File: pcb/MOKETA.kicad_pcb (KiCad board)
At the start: 2 copper layers, 144.9 x 166.3 mm, 129 parts, among them SW43 Reset, U1 Pro_Micro

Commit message: fix
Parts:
- moved SW12 187.8 mm to (317.3, 114.4), turned to 15 degrees
- moved SW11 162.5 mm to (297.1, 112.3), turned to 15 degrees
- moved SW24 148.2 mm to (322.2, 132.7), turned to 15 degrees
- moved SW25 140.8 mm to (79.3, 151.1), turned to -15 degrees
- moved SW10 137.7 mm to (276.9, 110.4), turned to 15 degrees
- moved SW37 132.5 mm to (150.3, 179.8), turned to -15 degrees
- moved SW23 123.2 mm to (302.0, 130.7), turned to 15 degrees
- moved SW9 114.3 mm to (257.3, 110.8), turned to 15 degrees
- moved SW26 113.1 mm to (99.5, 149.0), turned to -15 degrees
- moved SW38 111.0 mm to (168.0, 187.1), turned to -15 degrees
- moved SW36 108.7 mm to (327.1, 151.1), turned to 15 degrees
- moved U1 107.2 mm to (203.2, 116.0)
- moved SW22 99.1 mm to (281.8, 128.8), turned to 15 degrees
- moved SW8 97.0 mm to (240.2, 120.3), turned to 15 degrees
- moved SW13 92.3 mm to (84.2, 132.7), turned to -15 degrees
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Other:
- board size 144.9 x 166.3 mm -> 280 x 115 mm

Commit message: add outline
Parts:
- added SW44: ~, moketa:BSI-10H, F.Cu at (340.2, 157.3)
- moved LED12 222.3 mm to (318.6, 119.3), turned to 15 degrees
- moved LED24 218.1 mm to (323.5, 137.7), turned to 15 degrees
- moved LED36 214.0 mm to (328.4, 156.0), turned to 15 degrees
- moved LED11 202.3 mm to (298.4, 117.3), turned to 15 degrees
- moved LED23 198.0 mm to (303.3, 135.6), turned to 15 degrees
- moved LED35 193.9 mm to (308.2, 153.9), turned to 15 degrees
- moved LED9 183.7 mm to (258.6, 115.7), turned to 15 degrees
- moved LED10 182.4 mm to (278.2, 115.4), turned to 15 degrees
- moved LED22 178.0 mm to (283.1, 133.7), turned to 15 degrees
- moved LED34 173.8 mm to (288.0, 152.1), turned to 15 degrees
- moved LED8 162.2 mm to (241.5, 125.2), turned to 15 degrees
- moved LED21 158.0 mm to (263.5, 134.0), turned to 15 degrees
- moved LED33 153.7 mm to (268.5, 152.4), turned to 15 degrees
- moved LED7 140.5 mm to (225.0, 136.9), turned to 15 degrees
- moved LED20 138.0 mm to (246.4, 143.6), turned to 15 degrees
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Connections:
- LED37 pad 3: unconnected-(LED37-VSS-Pad3) -> GND
- LED42 pad 3: unconnected-(LED42-VSS-Pad3) -> GND
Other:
- board size 280 x 115 mm -> 283.8 x 114.8 mm

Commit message: Basic routing
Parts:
- moved SW42 39.2 mm to (256.1, 177.6)
- moved LED42 39.2 mm to (257.4, 182.5)
- moved SW40 37.5 mm to (220.7, 192.2)
- moved LED40 37.5 mm to (222.0, 197.1)
- moved D16 8.12 mm to (138.8, 117.7), turned to 75 degrees
- moved D4 8.12 mm to (143.7, 99.4), turned to 75 degrees
- moved D29 8.12 mm to (151.0, 145.6), turned to 75 degrees
- moved D2 8.12 mm to (104.0, 100.9), turned to 75 degrees
- moved D6 8.12 mm to (177.4, 120.6), turned to 75 degrees
- moved D26 8.12 mm to (94.1, 137.6), turned to 75 degrees
- moved D18 8.12 mm to (172.5, 139.0), turned to 75 degrees
- moved D14 8.12 mm to (99.1, 119.3), turned to 75 degrees
- moved D17 8.12 mm to (155.9, 127.2), turned to 75 degrees
- moved D28 8.12 mm to (133.9, 136.1), turned to 75 degrees
- moved D30 8.12 mm to (167.6, 157.3), turned to 75 degrees
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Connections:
- LED39 pad 1: Net-(LED39-VDD) -> VCC
- LED40 pad 1: Net-(LED39-VDD) -> VCC
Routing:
- net VCC: track 0.00 -> 882.2 mm
- net C0: track 0.00 -> 256.9 mm, vias 0 -> 8
- net C1: track 0.00 -> 251.1 mm, vias 0 -> 7
- net C2: track 0.00 -> 249.0 mm, vias 0 -> 8
- net C4: track 0.00 -> 248.9 mm, vias 0 -> 8
- net C5: track 0.00 -> 245.2 mm, vias 0 -> 7
- net C3: track 0.00 -> 245.0 mm, vias 0 -> 7
- net R4: track 0.00 -> 129.4 mm
- net R0: track 0.00 -> 128.2 mm
- net R2: track 0.00 -> 127.4 mm
- net R1: track 0.00 -> 117.5 mm
- net R5: track 0.00 -> 116.4 mm
- net R3: track 0.00 -> 113.6 mm
- net R6: track 0.00 -> 96.6 mm
- net Net-(LED36-DIN): track 0.00 -> 90.5 mm
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- added copper zone on B.Cu, net GND
- added copper zone on F.Cu, net GND
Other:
- outline, holes or cut-outs redrawn

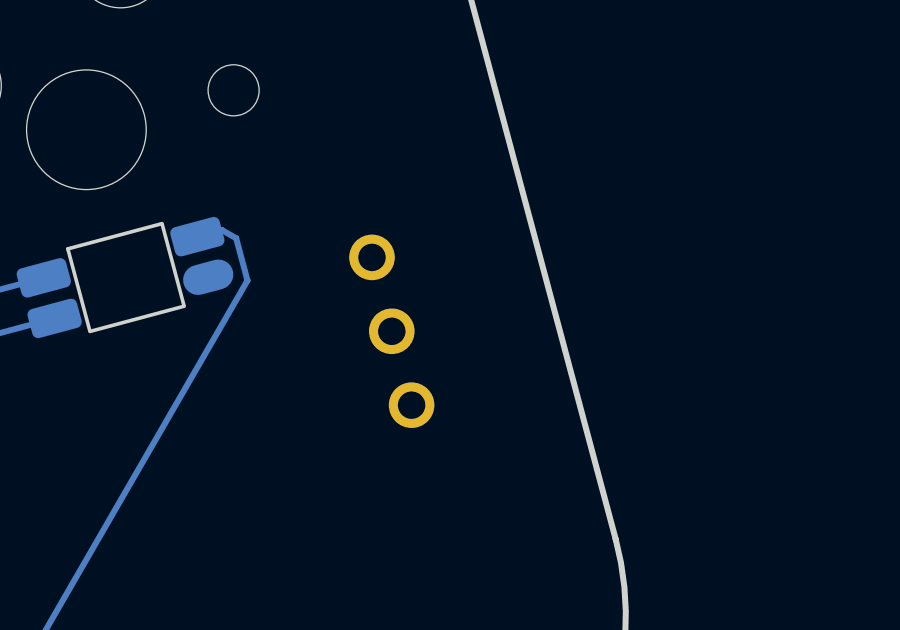
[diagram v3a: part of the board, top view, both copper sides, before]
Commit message: change footrpint
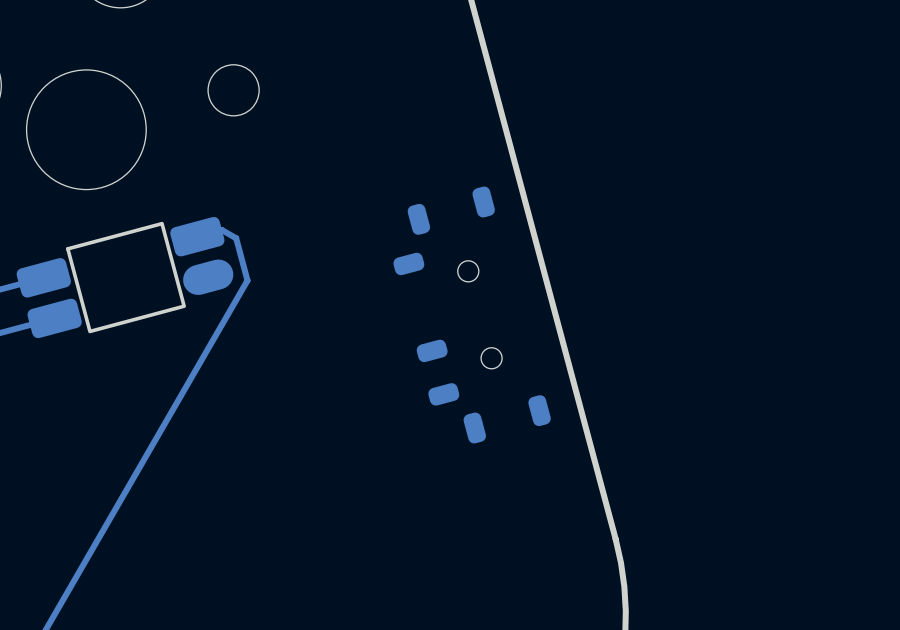
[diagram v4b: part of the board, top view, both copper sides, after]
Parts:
- SW44: footprint moketa:BSI-10H -> moketa:MSK-12C02

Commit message: add footrpint
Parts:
- added D43: ~, moketa:LED_1206, F.Cu at (63.3, 199.6)
- added D44: ~, moketa:LED_1206, F.Cu at (63.3, 203.0)
- added D45: ~, moketa:LED_1206, F.Cu at (63.3, 206.4)
- added D46: ~, moketa:LED_1206, F.Cu at (63.3, 209.8)
- added J2: ~, moketa:FFC_CMD_1x20_P0.5mm, F.Cu at (69.2, 192.3)
- added J3: ~, moketa:FFC_CMD_1x20_P0.5mm, F.Cu at (69.2, 197.1)
- added R1: ~, moketa:R_1206_3216, F.Cu at (69.2, 199.5)
- added R2: ~, moketa:R_1206_3216, F.Cu at (69.2, 202.9)
- added R3: ~, moketa:R_1206_3216, F.Cu at (69.2, 206.2)
- added R4: ~, moketa:R_1206_3216, F.Cu at (69.2, 209.5)
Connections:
- net LED renamed LEDS
- U1 pad 11: unconnected-(U1-8/B4-Pad11) -> LED2
- U1 pad 12: unconnected-(U1-9/B5-Pad12) -> LED3
- U1 pad 14: unconnected-(U1-B2/16-Pad14) -> LED4
- U1 pad 2: unconnected-(U1-RX1/D2-Pad2) -> LED1

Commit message: Doter pcb base cut
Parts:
- moved J3 147.6 mm to (203.2, 135.3)
- moved SW44 136.0 mm to (218.4, 94.6), turned to 0 degrees
- moved J2 135.2 mm to (203.6, 177.4), turned to 180 degrees
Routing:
- net C1: track 251.1 -> 231.9 mm
- net R1: track 117.5 -> 110.0 mm
- net C0: track 256.9 -> 249.7 mm
- net C3: track 245.0 -> 249.6 mm
- net R0: track 128.2 -> 123.9 mm
- net C2: track 249.0 -> 252.6 mm
- net R3: track 113.6 -> 117.1 mm
- net VCC: track 882.2 -> 884.3 mm
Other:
- outline, holes or cut-outs redrawn

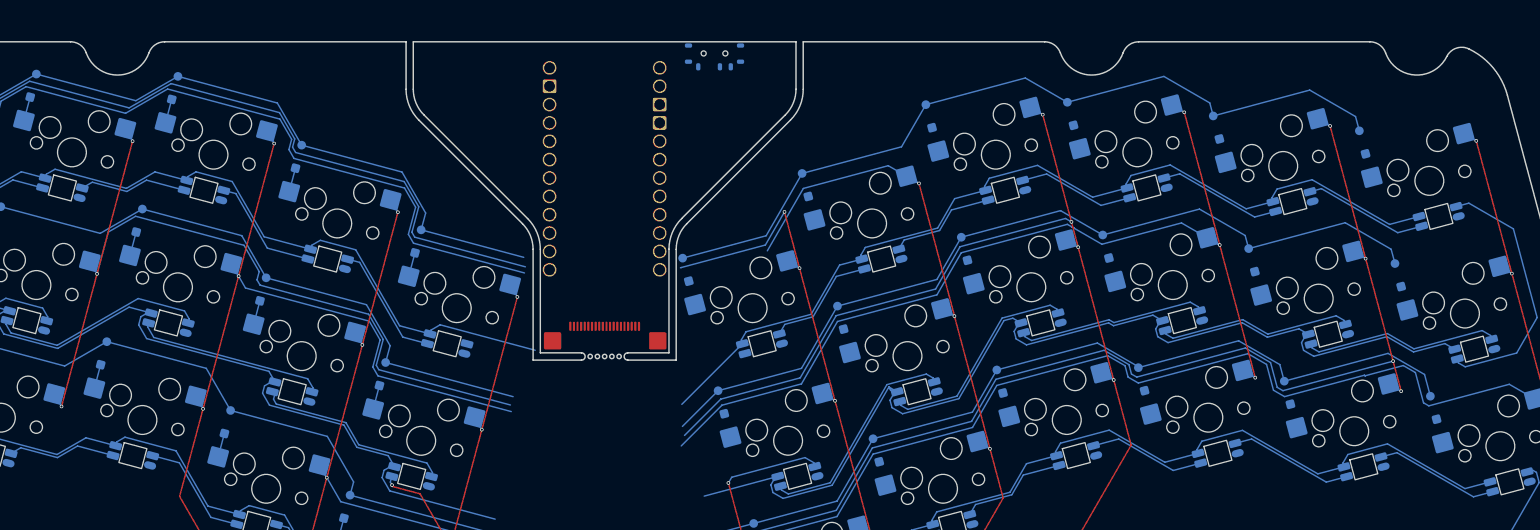
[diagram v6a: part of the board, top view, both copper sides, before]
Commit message: update footptint
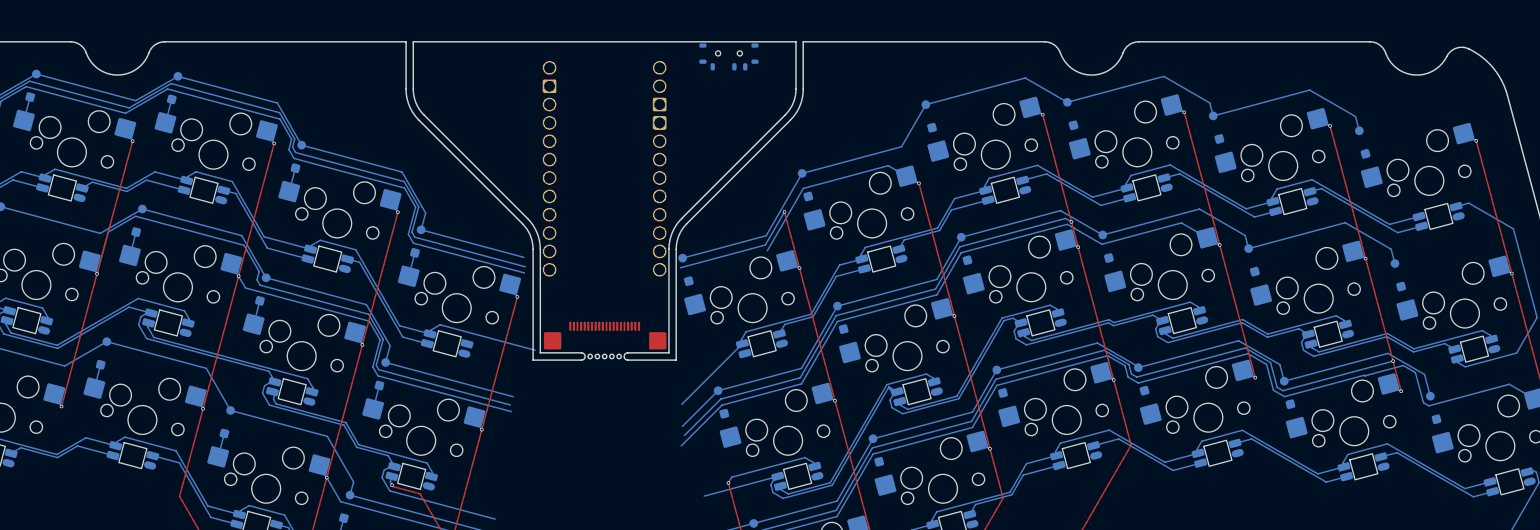
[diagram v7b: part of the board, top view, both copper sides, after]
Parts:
- moved SW44 2.00 mm to (220.4, 94.6)

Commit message: Basic routing on almost whole board
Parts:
- moved D46 283.3 mm to (332.7, 122.0), turned to 105 degrees
- moved D45 282.6 mm to (331.3, 116.7), turned to 105 degrees
- moved D44 281.9 mm to (329.9, 111.4), turned to 105 degrees
- moved D43 281.2 mm to (328.4, 106.1), turned to 105 degrees
- moved R4 244.3 mm to (311.2, 175.9), turned to 15 degrees
- moved R3 243.4 mm to (310.3, 172.3), turned to 15 degrees
- moved R2 242.5 mm to (309.3, 168.8), turned to 15 degrees
- moved R1 241.6 mm to (308.3, 165.2), turned to 15 degrees
- moved SW43 102.5 mm to (183.8, 98.2), turned to -120 degrees
- moved J1 60.7 mm to (203.5, 134.6)
- moved D40 38.3 mm to (211.5, 186.9)
- moved D42 38.3 mm to (246.9, 172.3)
- moved J2 0.35 mm to (203.2, 177.4)
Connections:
- D1 pad 1: R0 -> R0P
- D10 pad 1: R1 -> R1P
- D11 pad 1: R1 -> R1P
- D12 pad 1: R1 -> R1P
- D13 pad 1: R2 -> R2P
- D14 pad 1: R2 -> R2P
- D15 pad 1: R2 -> R2P
- D16 pad 1: R2 -> R2P
- D17 pad 1: R2 -> R2P
- D18 pad 1: R2 -> R2P
- D19 pad 1: R3 -> R3P
- D2 pad 1: R0 -> R0P
- D20 pad 1: R3 -> R3P
- D21 pad 1: R3 -> R3P
- D22 pad 1: R3 -> R3P
- D23 pad 1: R3 -> R3P
- D24 pad 1: R3 -> R3P
- D25 pad 1: R4 -> R4P
- D26 pad 1: R4 -> R4P
- D27 pad 1: R4 -> R4P
- D28 pad 1: R4 -> R4P
- D29 pad 1: R4 -> R4P
- D3 pad 1: R0 -> R0P
- D30 pad 1: R4 -> R4P
- D31 pad 1: R5 -> R5P
- D32 pad 1: R5 -> R5P
- D33 pad 1: R5 -> R5P
- D34 pad 1: R5 -> R5P
- D35 pad 1: R5 -> R5P
- D36 pad 1: R5 -> R5P
- D37 pad 1: R6 -> R6P
- D38 pad 1: R6 -> R6P
- D39 pad 1: R6 -> R6P
- D4 pad 1: R0 -> R0P
- D40 pad 1: R6 -> R6P
- D41 pad 1: R6 -> R6P
- D42 pad 1: R6 -> R6P
- D43 pad 1: GND -> GNDP
- D44 pad 1: GND -> GNDP
- D45 pad 1: GND -> GNDP
- D46 pad 1: GND -> GNDP
- D5 pad 1: R0 -> R0P
- D6 pad 1: R0 -> R0P
- D7 pad 1: R1 -> R1P
- D8 pad 1: R1 -> R1P
- D9 pad 1: R1 -> R1P
- J2 pad 1: unconnected-(J2-Pin_1-Pad1) -> LED3P
- J2 pad 10: unconnected-(J2-Pin_10-Pad10) -> LED1P
- J2 pad 11: unconnected-(J2-Pin_11-Pad11) -> LEDSP
- J2 pad 12: unconnected-(J2-Pin_12-Pad12) -> VCCP
- J2 pad 13: unconnected-(J2-Pin_13-Pad13) -> R1P
- J2 pad 14: unconnected-(J2-Pin_14-Pad14) -> R3P
- J2 pad 15: unconnected-(J2-Pin_15-Pad15) -> R5P
- J2 pad 16: unconnected-(J2-Pin_16-Pad16) -> C3P
- J2 pad 17: unconnected-(J2-Pin_17-Pad17) -> C4P
- J2 pad 18: unconnected-(J2-Pin_18-Pad18) -> C5P
- J2 pad 19: unconnected-(J2-Pin_19-Pad19) -> LED4P
- J2 pad 2: unconnected-(J2-Pin_2-Pad2) -> LED2P
- J2 pad 20: unconnected-(J2-Pin_20-Pad20) -> R6P
- J2 pad 3: unconnected-(J2-Pin_3-Pad3) -> C2P
- J2 pad 4: unconnected-(J2-Pin_4-Pad4) -> C1P
- J2 pad 5: unconnected-(J2-Pin_5-Pad5) -> C0P
- J2 pad 6: unconnected-(J2-Pin_6-Pad6) -> R4P
- J2 pad 7: unconnected-(J2-Pin_7-Pad7) -> R2P
- J2 pad 8: unconnected-(J2-Pin_8-Pad8) -> R0P
- J2 pad 9: unconnected-(J2-Pin_9-Pad9) -> GNDP
- J3 pad 1: unconnected-(J3-Pin_1-Pad1) -> R6D
- J3 pad 10: unconnected-(J3-Pin_10-Pad10) -> LEDSD
- J3 pad 11: unconnected-(J3-Pin_11-Pad11) -> LED1D
- J3 pad 12: unconnected-(J3-Pin_12-Pad12) -> GNDD
- J3 pad 13: unconnected-(J3-Pin_13-Pad13) -> R0D
- J3 pad 14: unconnected-(J3-Pin_14-Pad14) -> R2D
- J3 pad 15: unconnected-(J3-Pin_15-Pad15) -> R4D
- J3 pad 16: unconnected-(J3-Pin_16-Pad16) -> C0D
- J3 pad 17: unconnected-(J3-Pin_17-Pad17) -> C1D
- J3 pad 18: unconnected-(J3-Pin_18-Pad18) -> C2D
- J3 pad 19: unconnected-(J3-Pin_19-Pad19) -> LED2D
- J3 pad 2: unconnected-(J3-Pin_2-Pad2) -> LED4D
- J3 pad 20: unconnected-(J3-Pin_20-Pad20) -> LED3D
- J3 pad 3: unconnected-(J3-Pin_3-Pad3) -> C5D
- J3 pad 4: unconnected-(J3-Pin_4-Pad4) -> C4D
- J3 pad 5: unconnected-(J3-Pin_5-Pad5) -> C3D
- J3 pad 6: unconnected-(J3-Pin_6-Pad6) -> R5D
- J3 pad 7: unconnected-(J3-Pin_7-Pad7) -> R3D
- J3 pad 8: unconnected-(J3-Pin_8-Pad8) -> R1D
- J3 pad 9: unconnected-(J3-Pin_9-Pad9) -> VCCD
- LED1 pad 1: VCC -> VCCP
- LED1 pad 3: GND -> GNDP
- LED10 pad 1: VCC -> VCCP
- LED10 pad 3: GND -> GNDP
- LED11 pad 1: VCC -> VCCP
- LED11 pad 3: GND -> GNDP
- LED12 pad 1: VCC -> VCCP
- LED12 pad 3: GND -> GNDP
- LED13 pad 1: VCC -> VCCP
- LED13 pad 3: GND -> GNDP
- LED14 pad 1: VCC -> VCCP
- LED14 pad 3: GND -> GNDP
- LED15 pad 1: VCC -> VCCP
- LED15 pad 3: GND -> GNDP
- LED16 pad 1: VCC -> VCCP
- LED16 pad 3: GND -> GNDP
- LED17 pad 1: VCC -> VCCP
- LED17 pad 3: GND -> GNDP
- LED18 pad 1: VCC -> VCCP
- LED18 pad 3: GND -> GNDP
- LED19 pad 1: VCC -> VCCP
- LED19 pad 3: GND -> GNDP
- LED2 pad 1: VCC -> VCCP
- LED2 pad 3: GND -> GNDP
- LED20 pad 1: VCC -> VCCP
- LED20 pad 3: GND -> GNDP
- LED21 pad 1: VCC -> VCCP
- LED21 pad 3: GND -> GNDP
- LED22 pad 1: VCC -> VCCP
- LED22 pad 3: GND -> GNDP
- LED23 pad 1: VCC -> VCCP
- LED23 pad 3: GND -> GNDP
- LED24 pad 1: VCC -> VCCP
- LED24 pad 3: GND -> GNDP
- LED25 pad 1: VCC -> VCCP
- LED25 pad 3: GND -> GNDP
- LED26 pad 1: VCC -> VCCP
- LED26 pad 3: GND -> GNDP
- LED27 pad 1: VCC -> VCCP
- LED27 pad 3: GND -> GNDP
- LED28 pad 1: VCC -> VCCP
- LED28 pad 3: GND -> GNDP
- LED29 pad 1: VCC -> VCCP
- LED29 pad 3: GND -> GNDP
- LED3 pad 1: VCC -> VCCP
- LED3 pad 3: GND -> GNDP
- LED30 pad 1: VCC -> VCCP
- LED30 pad 3: GND -> GNDP
- LED31 pad 1: VCC -> VCCP
- LED31 pad 3: GND -> GNDP
- LED32 pad 1: VCC -> VCCP
- LED32 pad 3: GND -> GNDP
- LED33 pad 1: VCC -> VCCP
- LED33 pad 3: GND -> GNDP
- LED34 pad 1: VCC -> VCCP
- LED34 pad 3: GND -> GNDP
- LED35 pad 1: VCC -> VCCP
- LED35 pad 3: GND -> GNDP
- LED36 pad 1: VCC -> VCCP
- LED36 pad 3: GND -> GNDP
- LED37 pad 1: VCC -> VCCP
- LED37 pad 3: GND -> GNDP
- LED38 pad 1: VCC -> VCCP
- LED38 pad 3: GND -> GNDP
- LED39 pad 1: VCC -> VCCP
- LED39 pad 3: GND -> GNDP
- LED4 pad 1: VCC -> VCCP
- LED4 pad 3: GND -> GNDP
- LED40 pad 1: VCC -> VCCP
- LED40 pad 3: GND -> GNDP
- LED41 pad 1: VCC -> VCCP
- LED41 pad 3: GND -> GNDP
- LED42 pad 1: VCC -> VCCP
- LED42 pad 3: GND -> GNDP
- LED5 pad 1: VCC -> VCCP
- LED5 pad 3: GND -> GNDP
- LED6 pad 1: VCC -> VCCP
- LED6 pad 3: GND -> GNDP
- LED6 pad 4: LEDS -> LEDSP
- LED7 pad 1: VCC -> VCCP
- LED7 pad 3: GND -> GNDP
- LED8 pad 1: VCC -> VCCP
- LED8 pad 3: GND -> GNDP
- LED9 pad 1: VCC -> VCCP
- LED9 pad 3: GND -> GNDP
- R1 pad 1: LED1 -> LED1P
- R2 pad 1: LED2 -> LED2P
- R3 pad 1: LED3 -> LED3P
- R4 pad 1: LED4 -> LED4P
- SW1 pad 1: C0 -> C0P
- SW10 pad 1: C3 -> C3P
- SW11 pad 1: C4 -> C4P
- SW12 pad 1: C5 -> C5P
- SW13 pad 1: C0 -> C0P
- SW14 pad 1: C1 -> C1P
- SW15 pad 1: C2 -> C2P
- SW16 pad 1: C3 -> C3P
- SW17 pad 1: C4 -> C4P
- SW18 pad 1: C5 -> C5P
- SW19 pad 1: C0 -> C0P
- SW2 pad 1: C1 -> C1P
- SW20 pad 1: C1 -> C1P
- SW21 pad 1: C2 -> C2P
- SW22 pad 1: C3 -> C3P
- SW23 pad 1: C4 -> C4P
- SW24 pad 1: C5 -> C5P
- SW25 pad 1: C0 -> C0P
- SW26 pad 1: C1 -> C1P
- SW27 pad 1: C2 -> C2P
- SW28 pad 1: C3 -> C3P
- SW29 pad 1: C4 -> C4P
- SW3 pad 1: C2 -> C2P
- SW30 pad 1: C5 -> C5P
- SW31 pad 1: C0 -> C0P
- SW32 pad 1: C1 -> C1P
- SW33 pad 1: C2 -> C2P
- SW34 pad 1: C3 -> C3P
- SW35 pad 1: C4 -> C4P
- SW36 pad 1: C5 -> C5P
- SW37 pad 1: C3 -> C3P
- SW38 pad 1: C4 -> C4P
- SW39 pad 1: C5 -> C5P
- SW4 pad 1: C3 -> C3P
- SW40 pad 1: C0 -> C0P
- SW41 pad 1: C1 -> C1P
- SW42 pad 1: C2 -> C2P
- SW5 pad 1: C4 -> C4P
- SW6 pad 1: C5 -> C5P
- SW7 pad 1: C0 -> C0P
- SW8 pad 1: C1 -> C1P
- SW9 pad 1: C2 -> C2P
- U1 pad 1: LEDS -> LEDSD
- U1 pad 10: C2 -> C2D
- U1 pad 11: LED2 -> LED2D
- U1 pad 12: LED3 -> LED3D
- U1 pad 13: R6 -> R6D
- U1 pad 14: LED4 -> LED4D
- U1 pad 15: C5 -> C5D
- U1 pad 16: C4 -> C4D
- U1 pad 17: C3 -> C3D
- U1 pad 18: R5 -> R5D
- U1 pad 19: R3 -> R3D
- U1 pad 2: LED1 -> LED1D
- U1 pad 20: R1 -> R1D
- U1 pad 21: VCC -> VCCD
- U1 pad 3: GND -> GNDD
- U1 pad 4: GND -> GNDD
- U1 pad 5: R0 -> R0D
- U1 pad 6: R2 -> R2D
- U1 pad 7: R4 -> R4D
- U1 pad 8: C0 -> C0D
- U1 pad 9: C1 -> C1D
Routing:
- net VCCP: track 0.00 -> 1174.4 mm, vias 0 -> 1
- net VCC: track 884.3 -> 0.00 mm
- net C0P: track 0.00 -> 352.2 mm, vias 0 -> 9
- net C1P: track 0.00 -> 345.8 mm, vias 0 -> 8
- net C2P: track 0.00 -> 325.6 mm, vias 0 -> 9
- net C3P: track 0.00 -> 321.0 mm, vias 0 -> 8
- net C4P: track 0.00 -> 301.5 mm, vias 0 -> 9
- net C5P: track 0.00 -> 295.8 mm, vias 0 -> 8
- net C2: track 252.6 -> 0.00 mm, vias 8 -> 0
- net C0: track 249.7 -> 0.00 mm, vias 8 -> 0
- net C3: track 249.6 -> 0.00 mm, vias 7 -> 0
- net C4: track 248.9 -> 0.00 mm, vias 8 -> 0
- net C5: track 245.2 -> 0.00 mm, vias 7 -> 0
- net C1: track 231.9 -> 0.00 mm, vias 7 -> 0
- net R0P: track 0.00 -> 193.6 mm, vias 0 -> 1
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- added copper zone on B.Cu, net GNDP
- added copper zone on F.Cu, net GNDP
- removed copper zone on B.Cu, net GND
- removed copper zone on F.Cu, net GND
